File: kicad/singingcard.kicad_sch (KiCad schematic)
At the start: 16 parts, among them J2 Audio_In, SW1 Button, U1 ISD3900FYI, U2 W25Q16JVSSIQ

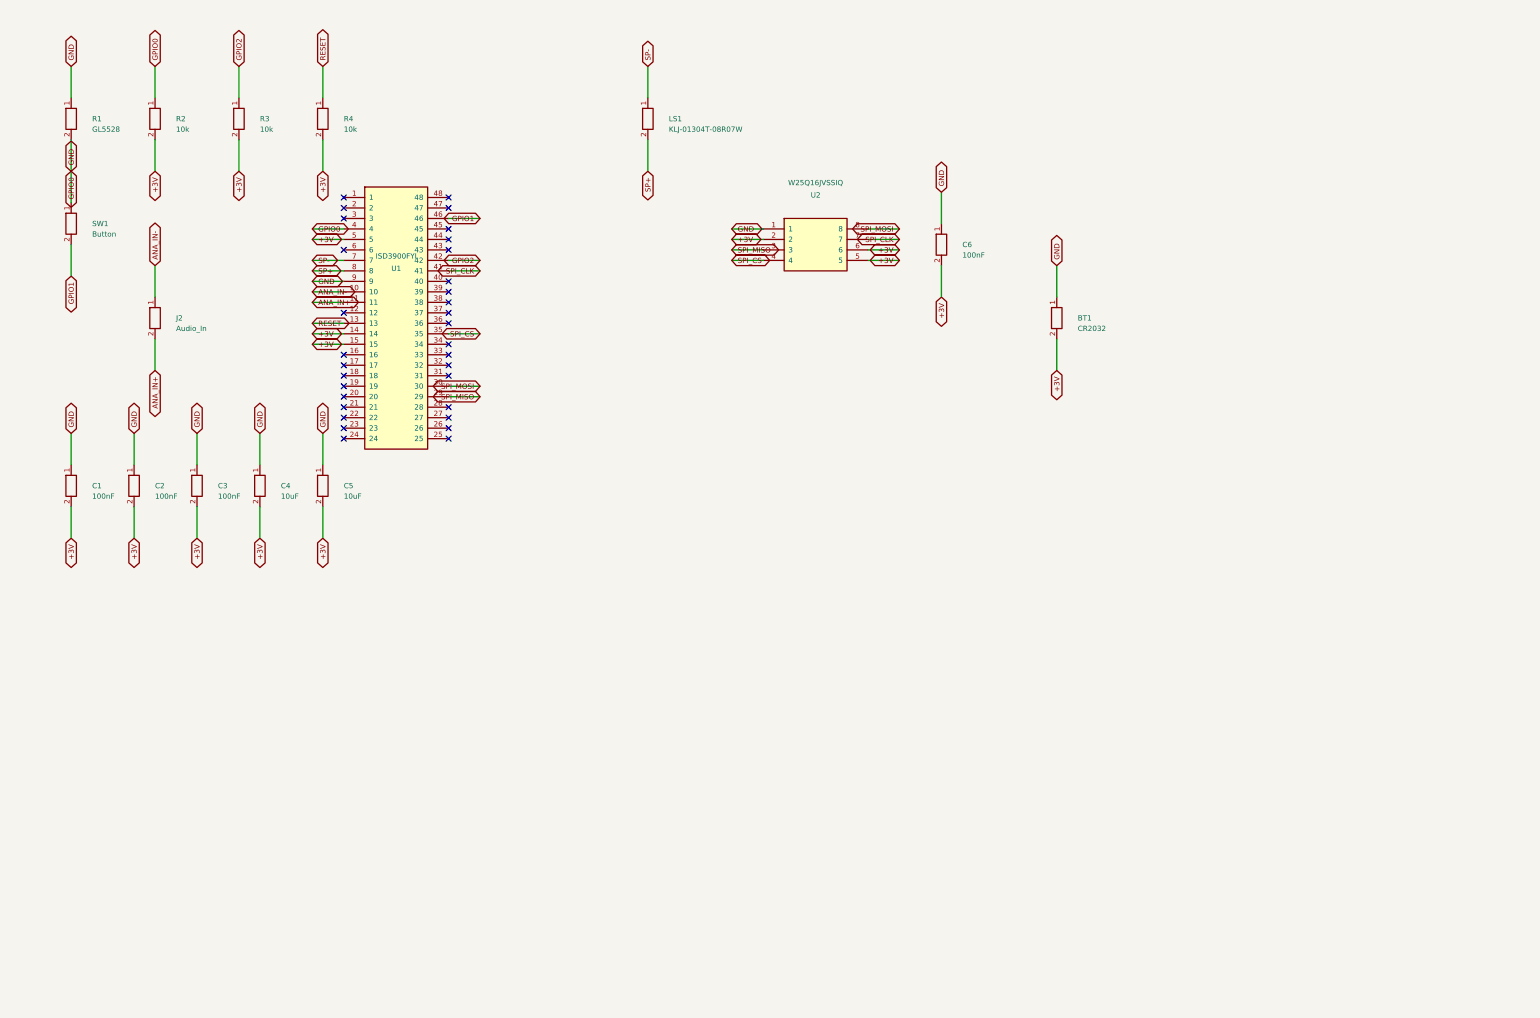
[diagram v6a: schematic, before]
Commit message: Improve schematic label layout significantly
Key fixes:
- Flipped label angles for IC pins (angle 0→180, 180→0)
  so wire connects to label tip, not through label text
- 4-level stagger for IC labels (pins mod 4) with 12.7mm spacing
  to spread labels horizontally and prevent overlap
- A3 page size with spread-out component layout
- Grid-aligned component positions (2.54mm grid)

Label placement logic:
- Left-side IC pins: label left of pin, angle 180 (text extends right)
- Right-side IC pins: label right of pin, angle 0 (text extends left)
- Stagger offset: 5.08 + (pin_num % 4) * 12.7 mm

ERC: 0 errors, 12 warnings (library paths only)

🤖 Generated with [Claude Code](https://claude.com/claude-code)

Co-Authored-By: Claude <noreply@anthropic.com>
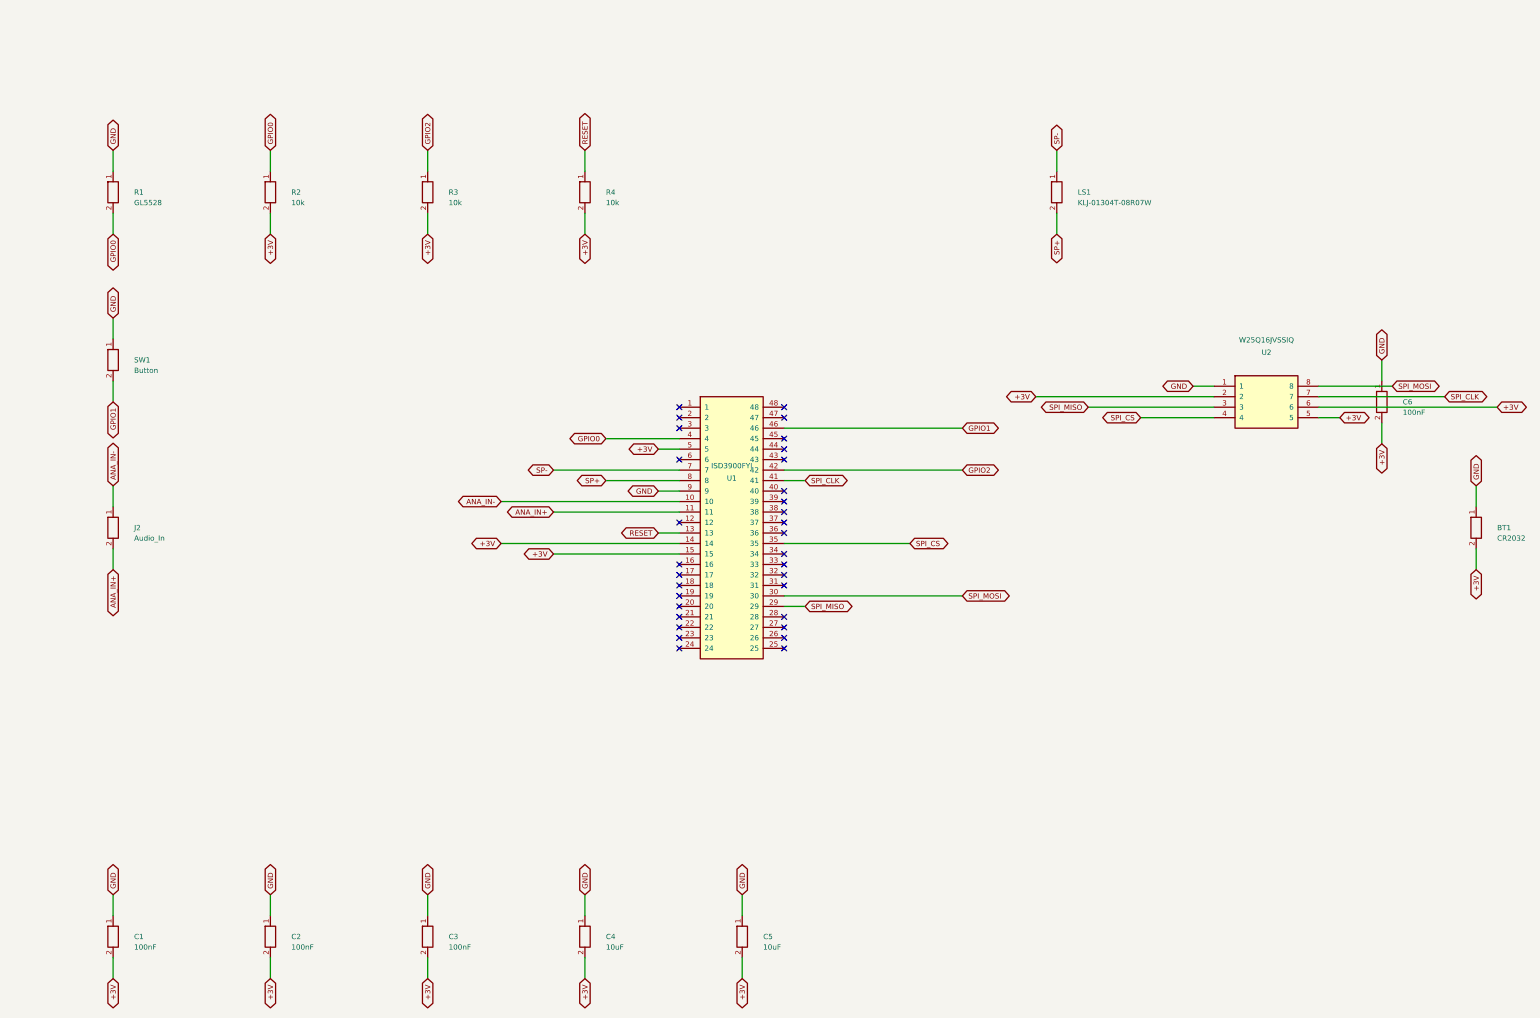
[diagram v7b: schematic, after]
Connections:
- net GND: no longer R1.2, R2.1, U1.4
- new net GPIO0: R1.2, R2.1, U1.4
